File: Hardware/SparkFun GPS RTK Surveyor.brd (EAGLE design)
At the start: 69.1 x 111.1 mm, 172 parts, among them J16 microSD, J3 USB-C, J4 Qwiic Right Angle, J6 Start Base, J7 Power Switch, Q2 MBT3904DW1T1, U1 MCP73831, U2 3.3V, U3 U-BLOX_ZED-F9P, U5 ESP-WROOM-32NARROW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

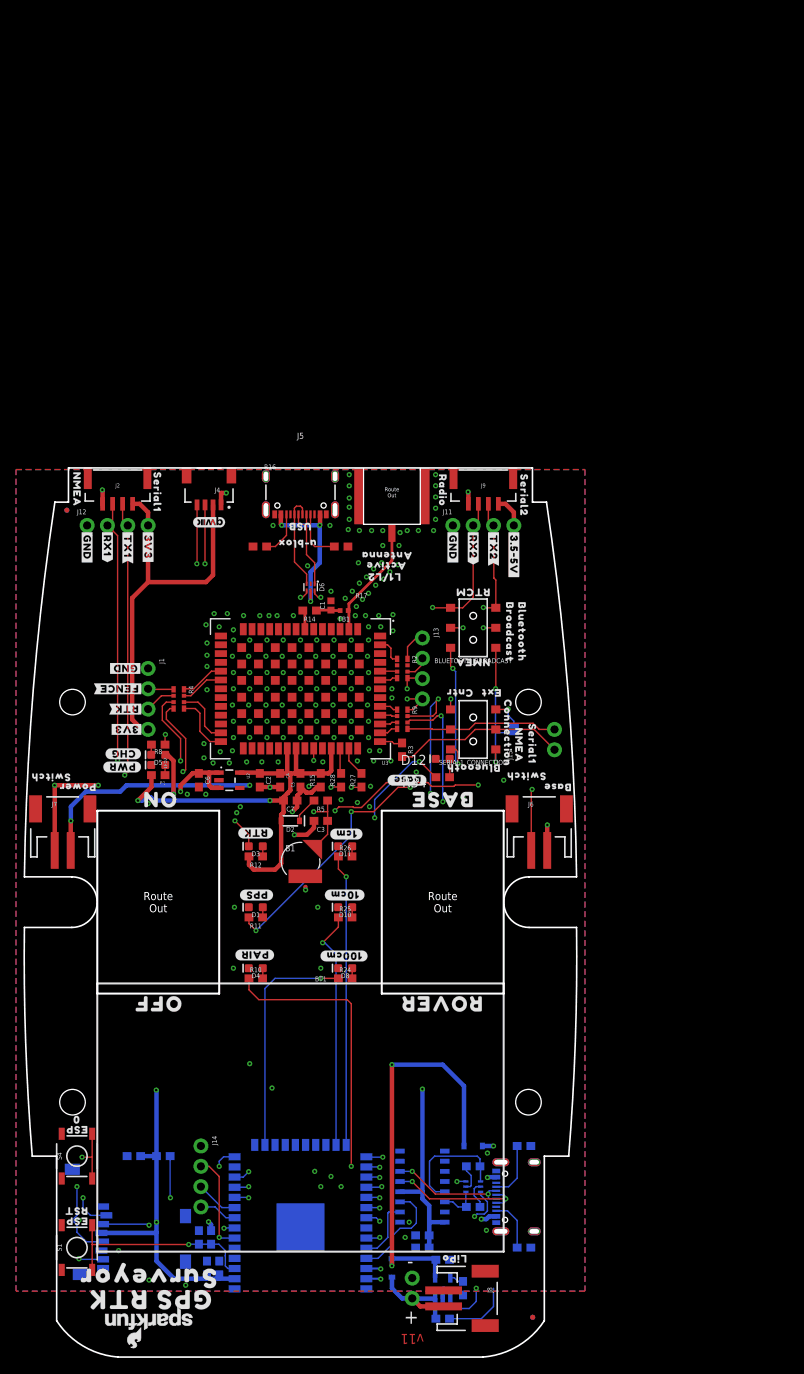
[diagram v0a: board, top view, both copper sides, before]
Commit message: v12. Add fuel guage. Move ESP32 connectors to panel edge.
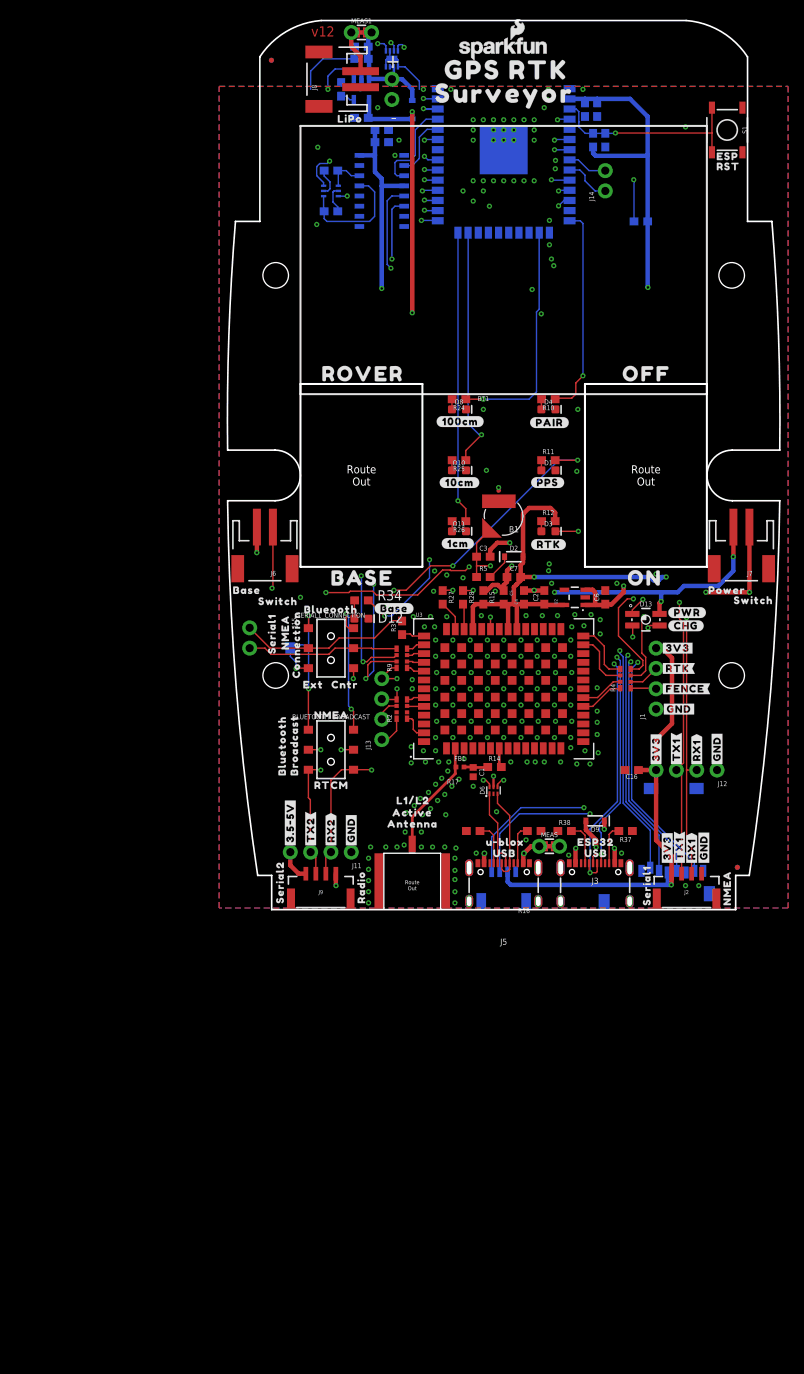
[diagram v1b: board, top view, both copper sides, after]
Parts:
- removed D5: Yellow, SparkFun-LED:LED-0603
- removed LED2: RED, SparkFun-LED:LED-0603
- removed R1, R8: 330, SparkFun-Resistors:0603
- removed S4: Boot, SparkFun-Switches:TACTILE_SWITCH_SMD_5.2MM
- added C15: 0.1uF, SparkFun-Capacitors:0603
- added D13: RGB, SparkFun-LED:P-LCC-4-3
- added MEAS, MEAS1: (no value), SparkFun-Jumpers:COMBO-JUMPER_2_NC_TRACE
- added U$66: (no value), output:USB1
- added U$67: (no value), output:ESP320
- added U$68: (no value), output:#RX1#2
- added U$82: (no value), output:#GND#0
- added U$83: (no value), output:MICROSD0
- added U7: MAX17048, SparkFun-IC-Power:DFN-8
- J14: device SparkFun-Connectors:1X04_NO_SILK -> SparkFun-Connectors:1X02_NO_SILK
- U$5: device output:ESP0 -> output:#3V3#0
- U$65: device output:02 -> output:#TX1#1
- moved LOGO3 164.9 mm to (25.4, 106.7), turned to 0 degrees
- moved S1 161.6 mm to (53.3, 96.5), turned to 270 degrees
- moved JP61 160.5 mm to (-3.63, 105.2), turned to 0 degrees
- moved JP81 160.5 mm to (-3.63, 105.2), turned to 0 degrees
- moved C8 157.8 mm to (7.62, 105.4), turned to 0 degrees
- moved U$70 155.8 mm to (16.3, 104.0), turned to 0 degrees
- moved U$74 153.9 mm to (51.3, 93.2), turned to 0 degrees
- moved J8 153.4 mm to (3.81, 102.9), turned to 90 degrees
- moved C13 152.8 mm to (37.1, 99.1), turned to 270 degrees
- moved J10 152.4 mm to (11.4, 102.9), turned to 270 degrees
- moved C11 151.8 mm to (35.6, 99.1), turned to 270 degrees
- moved U$60 151.7 mm to (51.3, 91.9), turned to 0 degrees
- moved R7 150.6 mm to (5.08, 101.6), turned to 270 degrees
- moved U1 150.2 mm to (7.62, 101.6), turned to 180 degrees
- moved U$71 149.7 mm to (14.2, 101.1), turned to 0 degrees
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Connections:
- net !SAFE! renamed ZED_!SAFE!
- net ESP32_12/BLUETOOTH_STATUS renamed ESP_12/LED_BLUETOOTH
- net ESP32_13/POSACC3 renamed ESP_13/LED_100CM
- net ESP32_15/POSACC2 renamed ESP_15/LED_10CM
- net ESP32_2/POSACC1 renamed ESP_2/LED_1CM
- net ESP32_4/BASE_STAT renamed ESP_4/LED_BASE_STAT
- net ESP32_5/BASE_SELECT renamed ESP_5/SWITCH_BASE_SELECT
- net ESP32_I39 renamed ESP_I39
- net ESP32_IO14_SCK1 renamed ESP_14
- net ESP32_IO16_RXI2 renamed ESP_16/BT_RXI
- net ESP32_IO17_TXO2 renamed ESP_17/BT_TXO
- net ESP32_IO18_SCK0 renamed ESP_18/SD_SCK
- net ESP32_IO19_CIPO0 renamed ESP_19/SD_CIPO
- net ESP32_IO23_COPI0 renamed ESP_23/SD_COPI
- net ESP32_IO25/!CS! renamed ESP_25/SD_!CS!
- net ESP32_IO26/TX_READY renamed ESP_26/ZED_TX_READY
- net ESP32_IO27/ZED-!RESET! renamed ESP_27/ZED_!RESET!
- net FENCE_STAT renamed ZED_FENCE_STAT
- net PPS_STAT renamed ZED_PPS_STAT
- net RTK_STAT renamed ZED_RTK_STAT
- removed net ESP32_I34: J14.2, U5.6
- removed net ESP32_I35: J14.1, U5.7
- removed net ESP32_I36: U5.4
- removed net ESP32_IO0: Q2.6, S4.3, S4.4, U5.25
- removed net ESP32_IO32: J14.4, U5.8
- removed net ESP32_IO33: J14.3, U5.9
- removed net N$10: LED2.A, R1.1
- removed net N$8: D5.C, R8.2
- removed net SCL: J4.4, R9.P7, U5.36
- removed net SDA: J4.3, R9.P6, U5.33
- new net ESP_0/BOOT: Q2.6, U5.25
- new net ESP_21/SDA: J4.3, R9.P6, U5.33, U7.8
- new net ESP_22/SCL: J4.4, R9.P7, U5.36, U7.7
- new net ESP_32: J14.2, U5.8
- new net ESP_33: J14.1, U5.9
- new net ESP_34/PWR_LVL_RED: D13.1, U5.6
- new net ESP_35/PWR_LVL_GRN: D13.2, U5.7
- new net ESP_36/BATT_ALRT: U5.4, U7.5
- new net N$4: J5.VBUS1, J5.VBUS2, MEAS.1, MEAS.3
- new net N$7: J8.2, MEAS1.1, MEAS1.3
- net 3.3V: no longer R1.2
- net CHG_LED: now also D13.3; no longer R8.1
- net GND: now also C15.2, U7.1, U7.4, U7.6, U7.9; no longer LED2.C, S4.1, S4.2
- net VIN: now also D13.4, MEAS.2, MEAS.4; no longer D5.A, J5.VBUS1, J5.VBUS2
- net V_BATT: now also C15.1, MEAS1.2, MEAS1.4, U7.2, U7.3; no longer J8.2
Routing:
- net ESP_22/SCL: track 0.00 -> 170.4 mm, vias 0 -> 7
- net ESP_21/SDA: track 0.00 -> 164.3 mm, vias 0 -> 7
- net SCL: track 149.9 -> 0.00 mm, vias 6 -> 0
- net SDA: track 139.4 -> 0.00 mm, vias 6 -> 0
- net D-1: track 15.1 -> 114.2 mm, vias 2 -> 4
- net D+1: track 17.2 -> 114.6 mm, vias 2 -> 4
- net ESP_25/SD_!CS!: track 32.3 -> 110.8 mm
- net ESP_23/SD_COPI: track 43.5 -> 121.9 mm
- net ESP_35/PWR_LVL_GRN: track 0.00 -> 70.0 mm, vias 0 -> 2
- net ESP_34/PWR_LVL_RED: track 0.00 -> 69.7 mm, vias 0 -> 2
- net ESP_19/SD_CIPO: track 49.7 -> 116.8 mm
- net ESP_18/SD_SCK: track 51.4 -> 114.3 mm, vias 2 -> 3
- net ESP32_IO0: track 58.2 -> 0.00 mm, vias 3 -> 0
- net ESP_36/BATT_ALRT: track 0.00 -> 35.3 mm, vias 0 -> 3
- net ESP_12/LED_BLUETOOTH: track 54.6 -> 26.4 mm, vias 2 -> 1
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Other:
- outline, holes or cut-outs redrawn
- board text added: "v12"
- board text removed: "Measurements in inches"
- board text removed: "v11"

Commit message: v13 hardware. Fix power LED. Add gcode for enclosure.
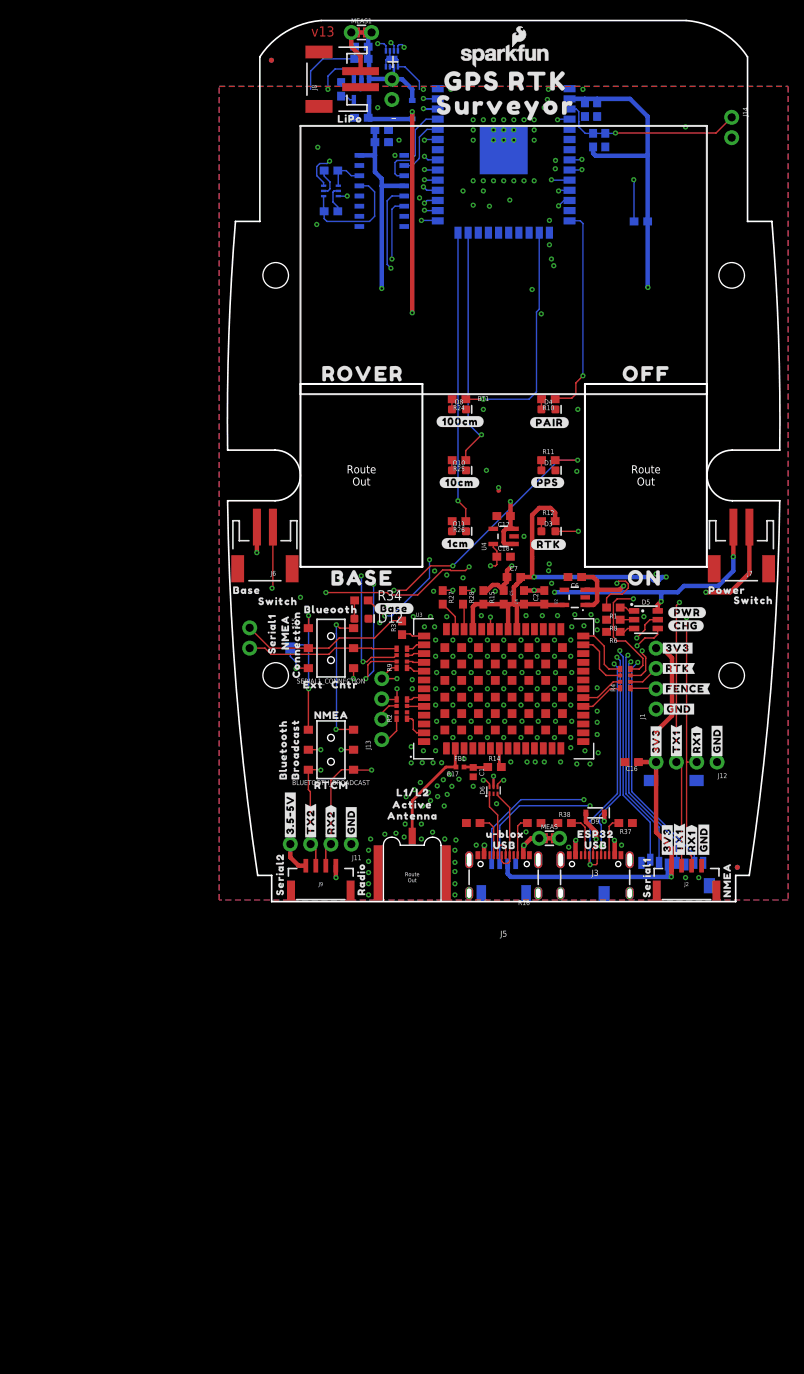
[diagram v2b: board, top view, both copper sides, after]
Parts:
- removed B1: 6.8MM_COIN_CELL, SparkFun-Batteries:ML414H_IV01E
- removed C3: 1.0uF, SparkFun-Capacitors:0603
- removed D13: RGB, SparkFun-LED:P-LCC-4-3
- removed D2: 0.5A/40V/420mV, SparkFun-DiscreteSemi:SOD-323
- removed R5: 3.3k, SparkFun-Resistors:0603
- removed S1: RESET, SparkFun-Switches:TACTILE_SWITCH_SMD_5.2MM
- removed U$74: (no value), output:ESP0
- added C17, C18: 1.0uF, SparkFun-Capacitors:0603
- added D5: RGB, SparkFun-LED:PLCC-6-LED
- added R1: 1k, SparkFun-Resistors:0603
- added R6, R8: 330, SparkFun-Resistors:0603
- added U$84: (no value), output:#GND#1
- added U4: 3.3V, SparkFun-IC-Power:SOT23-5
- U$60: device output:RST1 -> output:#ESP_RST#0
- moved J14 18.3 mm to (53.9, 98.1), turned to 270 degrees
- moved U$60 6.43 mm to (53.3, 98.0), flipped to the bottom
- moved C6 4.58 mm to (34.3, 40.6), turned to 180 degrees
- moved U$83 2.00 mm to (52.6, 14.8)
- moved U$71 1.50 mm to (14.4, 99.6)
- moved U$70 1.41 mm to (16.2, 102.6)
- moved C16 1.00 mm to (41.4, 17.5)
- moved D9 1.00 mm to (36.8, 11.2)
- moved E1 1.00 mm to (14.0, 0.11)
- moved J11 1.00 mm to (6.35, 7.25)
- moved J12 1.00 mm to (52.1, 17.5)
- moved J16 1.00 mm to (51.6, 15.6)
- moved J2 1.00 mm to (48.3, 1.25)
- moved J3 1.00 mm to (36.8, 6.21)
- moved J5 1.00 mm to (25.4, 6.21)
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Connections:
- removed net ESP_32: J14.2, U5.8
- removed net ESP_33: J14.1, U5.9
- removed net ESP_34/PWR_LVL_RED: D13.1, U5.6
- removed net ESP_35/PWR_LVL_GRN: D13.2, U5.7
- removed net N$6: D2.C, R5.2
- new net ESP_32/PWR_LVL_RED: D5.AR, U5.8
- new net ESP_33/PWR_LVL_GRN: D5.AG, U5.9
- new net ESP_I34: U5.6
- new net ESP_I35: U5.7
- new net N$10: D5.CG, R6.1
- new net N$14: D5.CR, R8.1
- new net N$17: D5.CB, R1.1
- net 3.3V: no longer D2.A
- net BACKUP: now also C18.1, U4.5; no longer B1.+, C3.1, R5.1
- net CHG_LED: now also R1.2; no longer D13.3
- net ESP32_EN: now also J14.1; no longer S1.3, S1.4
- net ESP_16/BT_RXI: now also BLUETOOTH_BROADCAST.2; no longer BLUETOOTH_BROADCAST.5
- net ESP_17/BT_TXO: now also BLUETOOTH_BROADCAST.5; no longer BLUETOOTH_BROADCAST.2
- net EXTERNAL_SERIAL1_RXI: now also SERIAL1_CONNECTION.4; no longer SERIAL1_CONNECTION.3
- net EXTERNAL_SERIAL1_TXO: now also SERIAL1_CONNECTION.1; no longer SERIAL1_CONNECTION.6
- net GND: now also C17.2, C18.2, J14.2, R6.2, R8.2, U4.2; no longer B1.-, C3.2, S1.1, S1.2
- net NMEA-RX: now also BLUETOOTH_BROADCAST.6, SERIAL1_CONNECTION.6; no longer BLUETOOTH_BROADCAST.1, SERIAL1_CONNECTION.1
- net NMEA-TX: now also BLUETOOTH_BROADCAST.3, SERIAL1_CONNECTION.3; no longer BLUETOOTH_BROADCAST.4, SERIAL1_CONNECTION.4
- net VIN: now also D5.AB; no longer D13.4
- net V_BATT: now also C17.1, U4.1, U4.3
- net ZED-RXI1: now also SERIAL1_CONNECTION.5; no longer SERIAL1_CONNECTION.2
- net ZED-RXI2: now also BLUETOOTH_BROADCAST.4; no longer BLUETOOTH_BROADCAST.3
- net ZED-TXO1: now also SERIAL1_CONNECTION.2; no longer SERIAL1_CONNECTION.5
- net ZED-TXO2: now also BLUETOOTH_BROADCAST.1; no longer BLUETOOTH_BROADCAST.6
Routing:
- net V_BATT: track 16.3 -> 89.5 mm, vias 0 -> 3
- net ESP_32/PWR_LVL_RED: track 0.00 -> 71.6 mm, vias 0 -> 2
- net ESP_33/PWR_LVL_GRN: track 0.00 -> 70.8 mm, vias 0 -> 2
- net ESP_35/PWR_LVL_GRN: track 70.0 -> 0.00 mm, vias 2 -> 0
- net ESP_34/PWR_LVL_RED: track 69.7 -> 0.00 mm, vias 2 -> 0
- net ESP_33: track 5.97 -> 0.00 mm
- net 5V: track 118.0 -> 112.3 mm, vias 3 -> 2
- net CHG_LED: track 113.0 -> 107.9 mm, vias 5 -> 4
- net ESP_32: track 5.02 -> 0.00 mm
- net BACKUP: track 15.8 -> 11.5 mm
- net GND: track 37.7 -> 34.1 mm, vias 189 -> 190
- net N$6: track 3.29 -> 0.00 mm
- net 3.3V: track 259.9 -> 257.6 mm
- net ESP32_EN: track 67.9 -> 65.6 mm
- net VIN: track 186.6 -> 184.4 mm
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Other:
- board size 69.1 x 111.1 mm -> 69.1 x 110.1 mm
- board text added: "v13"
- board text removed: "v12"
